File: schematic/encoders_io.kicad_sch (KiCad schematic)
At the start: 4 parts, among them J40 ENC0, J41 ENC1, J42 ENC2, J43 ENC3

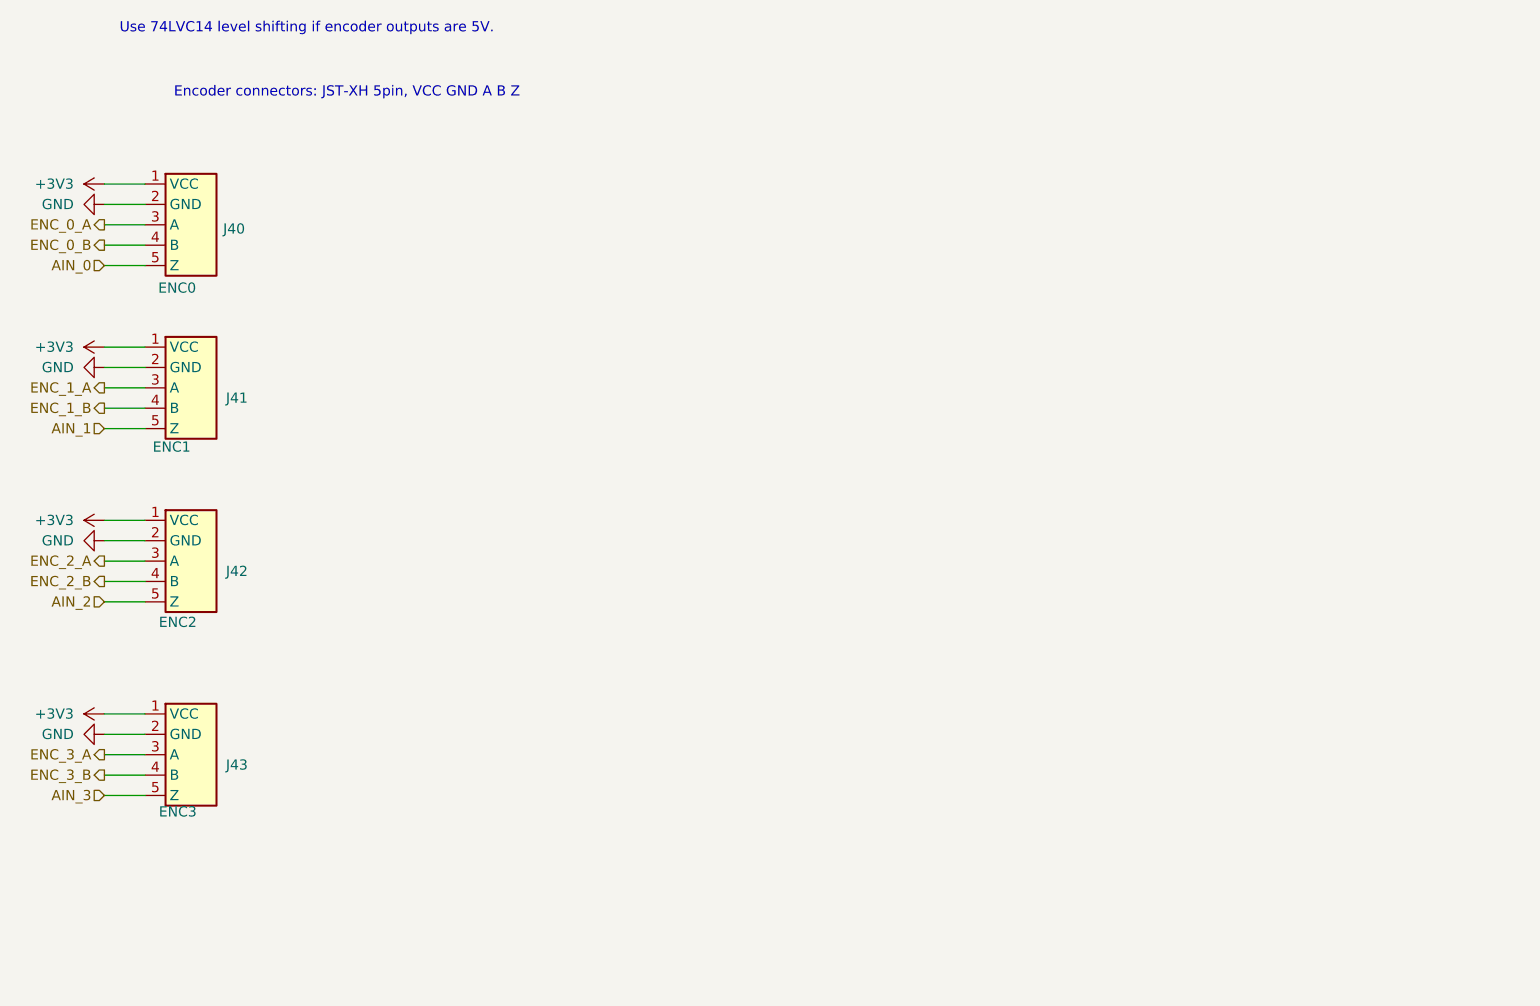
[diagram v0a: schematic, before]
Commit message: Redesign schematic to 3ch: DRV8825x3, AM26LV32 differential encoder, swap ADC3/ADC4
- DRV8825 stepper driver: 4ch -> 3ch (STEP/DIR CH0-2 on GPIO6-11)
- Encoder: 3ch differential input via AM26LV32IDR for Stepperonline 17HS15-1504-ME1K (1000PPR)
  - A+/A-, B+/B-, Z+/Z- differential pairs, GPIO15-17/18/21/35/36-37/40
- ADC assignment swap: GPIO4=MOT_V(ADC3) voltage monitor, GPIO5=CURRENT(ADC4) 100mOhm+20x amp
- Updated Gerber files (Gerber202960613 replaces Gerber202960504)
- Added AM26LV32IDR and AM26C32INSR library files
- Updated REQUIREMENTS.md: 3ch axis range, encoder specs, ADC channel table, current conversion formula
- Updated CLAUDE.md: corrected GPIO4/5 signal assignments and startup sequence

Co-Authored-By: Claude Sonnet 4.6 <noreply@anthropic.com>
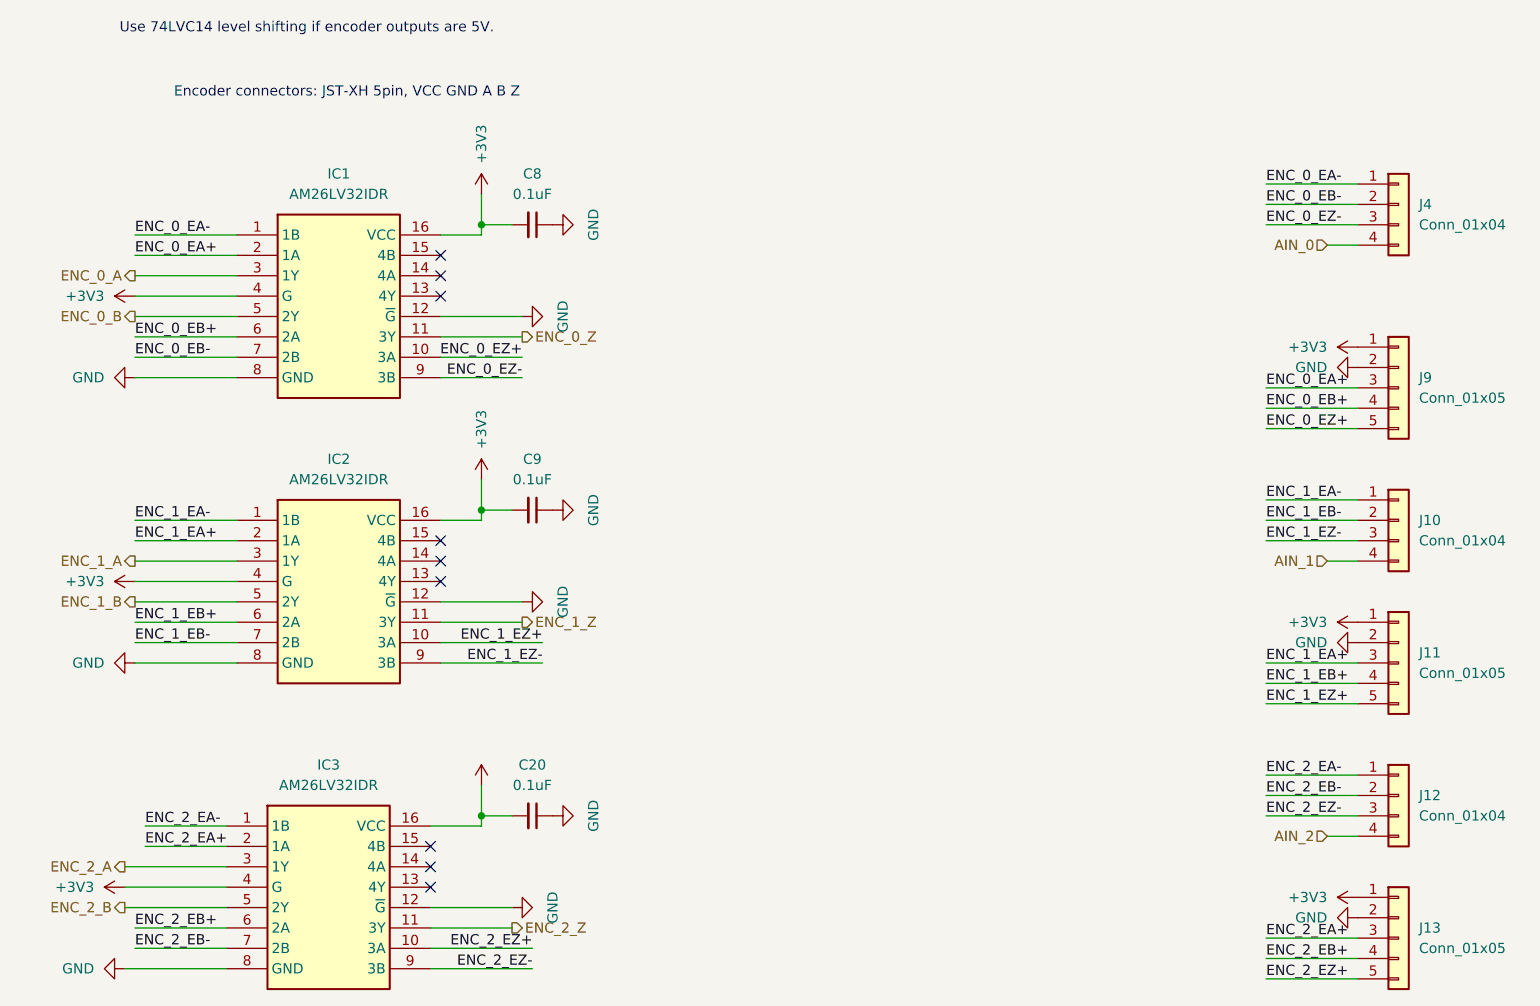
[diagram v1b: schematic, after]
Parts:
- removed J40: ENC0, Connector_JST:JST_PH_B5B-PH-K_1x05_P2.00mm_Vertical, symbol SteppingMotorDriver_symbols:ENCODER_CONN_1X5
- removed J41: ENC1, Connector_JST:JST_PH_B5B-PH-K_1x05_P2.00mm_Vertical, symbol SteppingMotorDriver_symbols:ENCODER_CONN_1X5
- removed J42: ENC2, Connector_JST:JST_PH_B5B-PH-K_1x05_P2.00mm_Vertical, symbol SteppingMotorDriver_symbols:ENCODER_CONN_1X5
- removed J43: ENC3, Connector_JST:JST_PH_B5B-PH-K_1x05_P2.00mm_Vertical, symbol SteppingMotorDriver_symbols:ENCODER_CONN_1X5
- added C20, C8, C9: 0.1uF, Capacitor_SMD:C_0603_1608Metric, symbol Device:C_Small
- added IC1, IC2, IC3: AM26LV32IDR, SOIC127P600X175-16N, symbol AM26LV32IDR:AM26LV32IDR
- added J10, J12, J4: Conn_01x04, Connector_JST:JST_PH_B4B-PH-K_1x04_P2.00mm_Vertical, symbol Connector_Generic:Conn_01x04
- added J11, J13, J9: Conn_01x05, Connector_JST:JST_PH_B5B-PH-K_1x05_P2.00mm_Vertical, symbol Connector_Generic:Conn_01x05
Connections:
- net +3V3: now also C20.2, C8.2, C9.2, IC1.16 (VCC), IC1.4 (G), IC2.16 (VCC), IC2.4 (G), IC3.16 (VCC), IC3.4 (G), J11.1 (Pin_1), J13.1 (Pin_1), J9.1 (Pin_1)
- net AIN_0: now also J4.4 (Pin_4)
- net AIN_1: now also J10.4 (Pin_4)
- net AIN_2: now also J12.4 (Pin_4)
- net ENC_0_A: now also IC1.3 (1Y)
- net ENC_0_B: now also IC1.5 (2Y)
- net ENC_1_A: now also IC2.3 (1Y)
- net ENC_1_B: now also IC2.5 (2Y)
- net ENC_2_A: now also IC3.3 (1Y)
- net ENC_2_B: now also IC3.5 (2Y)
- net GND: now also C20.1, C8.1, C9.1, IC1.12 (~{G}), IC1.8 (GND), IC2.12 (~{G}), IC2.8 (GND), IC3.12 (~{G}), IC3.8 (GND), J11.2 (Pin_2), J13.2 (Pin_2), J9.2 (Pin_2)
- new net ENC_0_EA+: IC1.2 (1A), J9.3 (Pin_3)
- new net ENC_0_EA-: IC1.1 (1B), J4.1 (Pin_1)
- new net ENC_0_EB+: IC1.6 (2A), J9.4 (Pin_4)
- new net ENC_0_EB-: IC1.7 (2B), J4.2 (Pin_2)
- new net ENC_0_EZ+: IC1.10 (3A), J9.5 (Pin_5)
- new net ENC_0_EZ-: IC1.9 (3B), J4.3 (Pin_3)
- new net ENC_0_Z: IC1.11 (3Y)
- new net ENC_1_EA+: IC2.2 (1A), J11.3 (Pin_3)
- new net ENC_1_EA-: IC2.1 (1B), J10.1 (Pin_1)
- new net ENC_1_EB+: IC2.6 (2A), J11.4 (Pin_4)
- new net ENC_1_EB-: IC2.7 (2B), J10.2 (Pin_2)
- new net ENC_1_EZ+: IC2.10 (3A), J11.5 (Pin_5)
- new net ENC_1_EZ-: IC2.9 (3B), J10.3 (Pin_3)
- new net ENC_1_Z: IC2.11 (3Y)
- new net ENC_2_EA+: IC3.2 (1A), J13.3 (Pin_3)
- new net ENC_2_EA-: IC3.1 (1B), J12.1 (Pin_1)
- new net ENC_2_EB+: IC3.6 (2A), J13.4 (Pin_4)
- new net ENC_2_EB-: IC3.7 (2B), J12.2 (Pin_2)
- new net ENC_2_EZ+: IC3.10 (3A), J13.5 (Pin_5)
- new net ENC_2_EZ-: IC3.9 (3B), J12.3 (Pin_3)
- new net ENC_2_Z: IC3.11 (3Y)
- no-connect marks 0 -> 9
